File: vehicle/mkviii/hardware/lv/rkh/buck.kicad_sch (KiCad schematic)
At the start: 5 parts, among them U3 AP63203WU-7

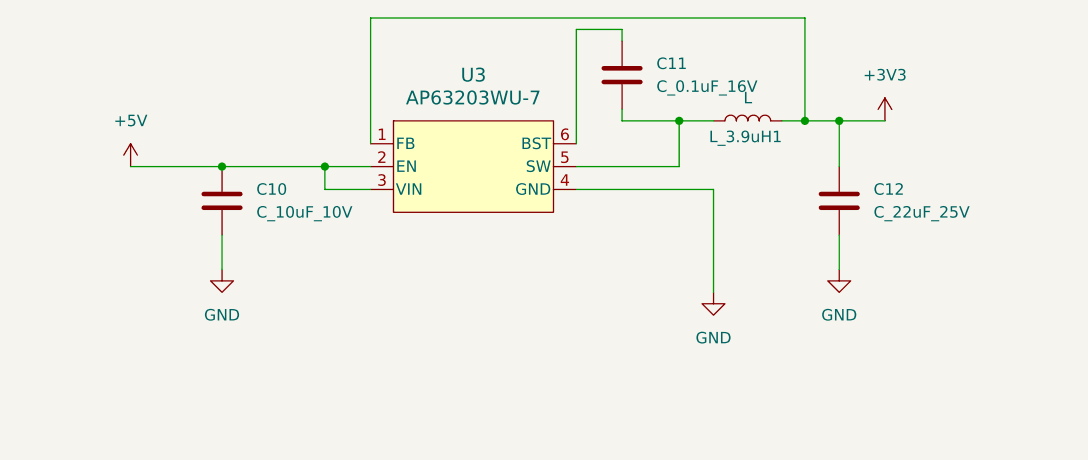
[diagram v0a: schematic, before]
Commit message: RKH - routed all non CAN traces.  Still need to do DRC overview
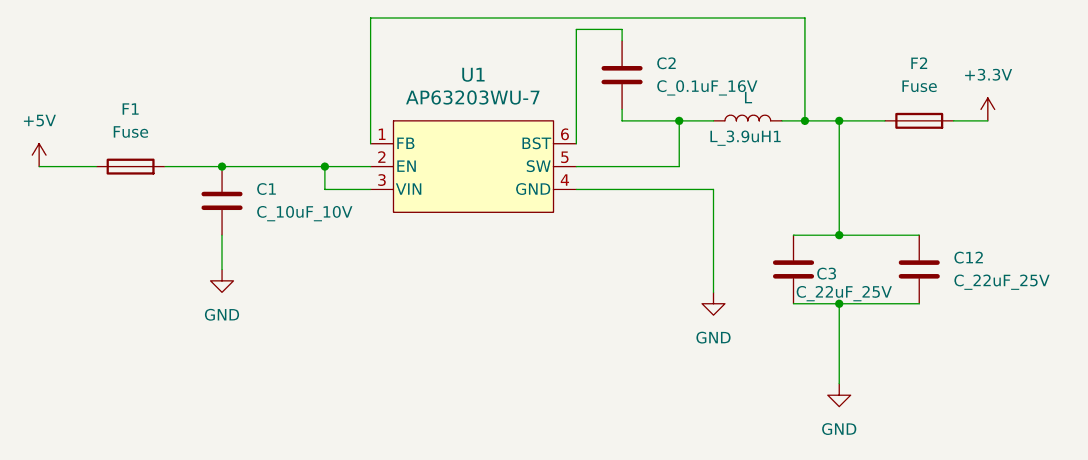
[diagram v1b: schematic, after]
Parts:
- added C12: C_22uF_25V, OEM:C_1206_3216Metric, symbol OEM:C_22uF_25V_1206
- added F1, F2: Fuse, OEM:Fuse_1210_3225Metric, symbol Device:Fuse
- L_3.9uH1: footprint (none) -> OEM:IND_BOURNS_SRR5018 (L_3.9uH_2A_55m_SMD)
- renumbered C10 to C1, C11 to C2, C12 to C3, U3 to U1
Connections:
- net +5V: now also F1.1; no longer C1.1, U1.2 (EN), U1.3 (VIN)
- net GND: now also C12.2
- net +3V3: no longer names the net of C3.1, L_3.9uH1.2, U1.1 (FB)
- net +3V3: now also C12.1, F2.1
- new net: C1.1, F1.2, U1.2 (EN), U1.3 (VIN)
- new net +3.3V: F2.2
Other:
- moved on the sheet: C3

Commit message: Added production files; rounded corners; added throttle power wire terminal
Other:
- title: (none) -> 5 V -> 3.3 V Buck Converter
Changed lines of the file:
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@@
 	(generator_version "9.0")
 	(paper "A4")
+	(title_block
+		(title "5 V -> 3.3 V Buck Converter")
+		(rev "1")
+		(comment 1 "Jack Goode")
+	)
 	(junction
 		(at 168.91 92.71)
